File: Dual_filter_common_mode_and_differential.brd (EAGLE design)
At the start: 61 x 38.1 mm, 23 parts

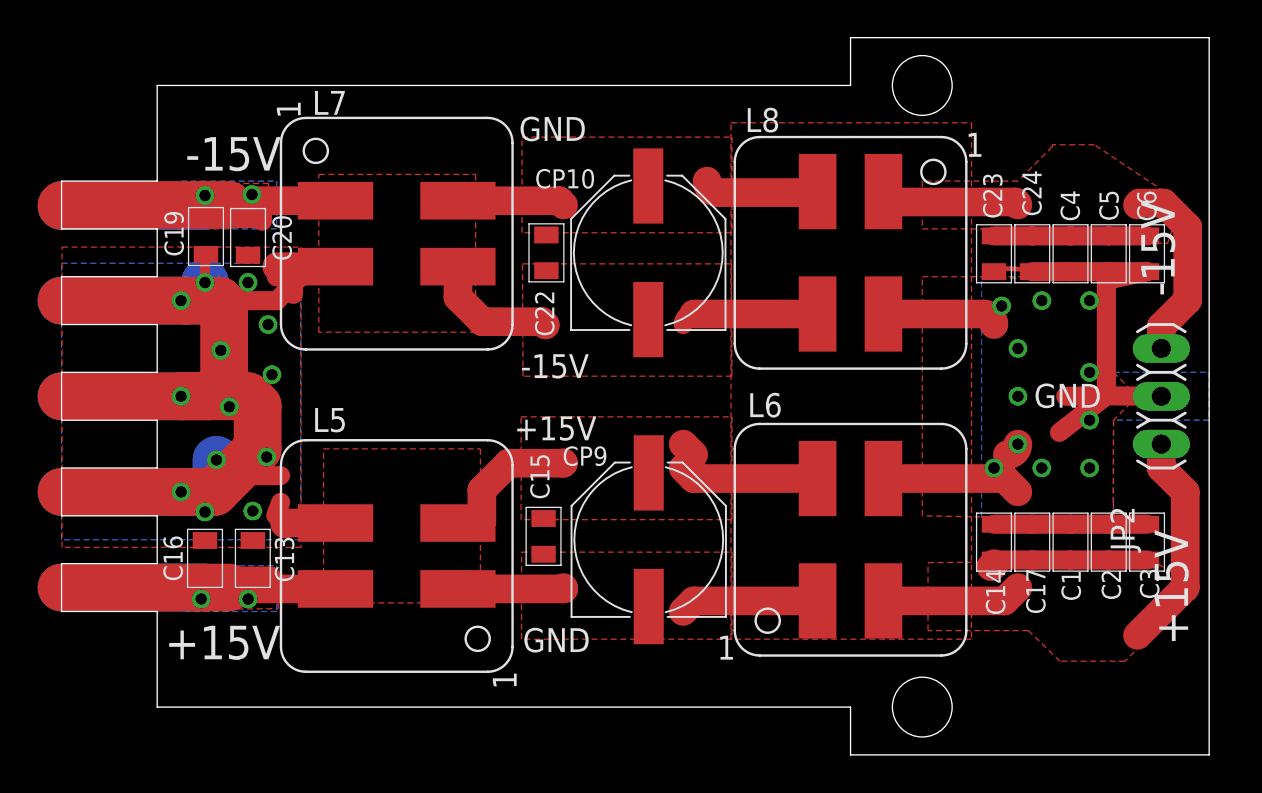
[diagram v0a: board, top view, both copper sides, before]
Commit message: Switched from CM-DIFF top CM-CM filtering
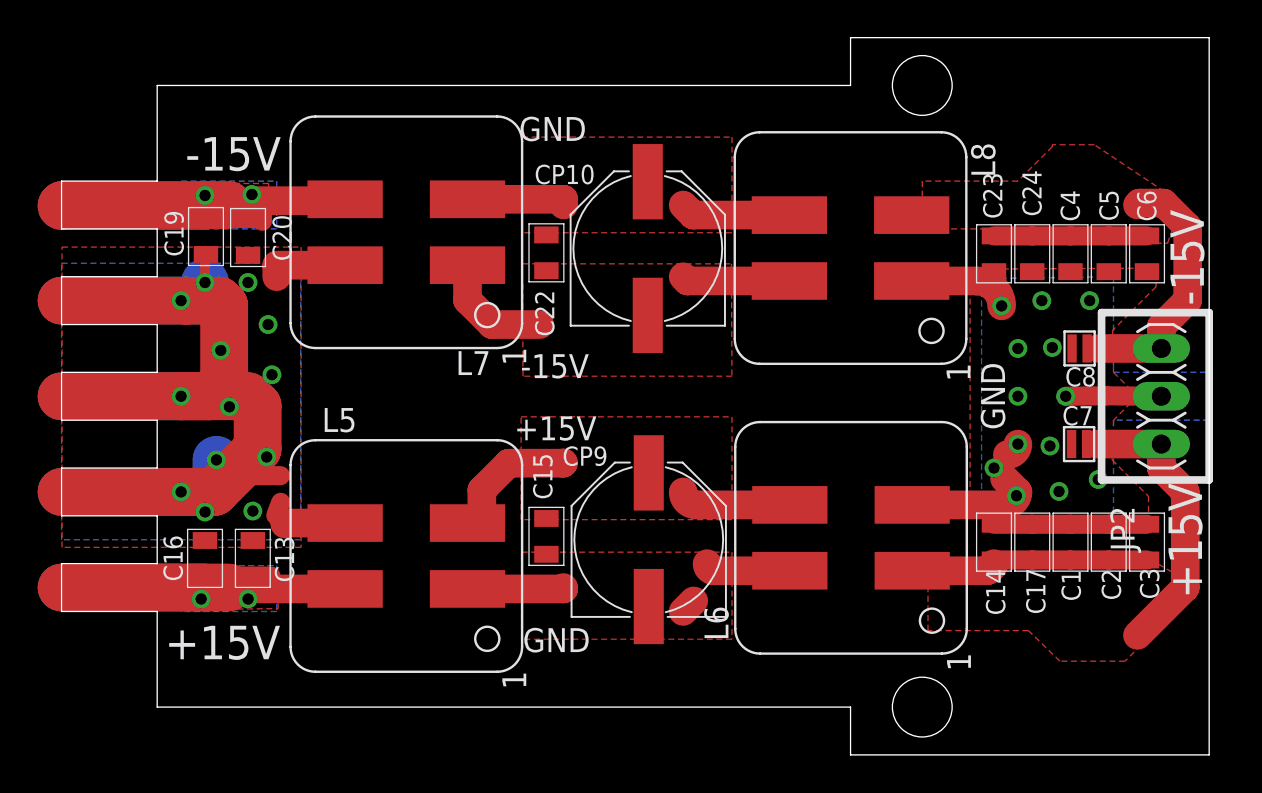
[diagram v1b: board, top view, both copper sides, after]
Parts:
- added C7, C8: 22nF, jqi_passives:C_MLCC_0306
- moved L7 0.51 mm to (19.6, 27.8), turned to 270 degrees
- moved L5 0.51 mm to (19.6, 10.6)
- moved L8 0.25 mm to (43.2, 26.9), turned to 270 degrees
- moved CP10 0.23 mm to (32.4, 26.9)
- moved C15 0.15 mm to (27.0, 11.6)
- moved L6 0.10 mm to (43.2, 11.5), turned to 270 degrees
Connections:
- net -15V2: now also L7.P$3; no longer L7.P$1
- net COM2: now also L7.P$4; no longer L7.P$2
- net GND2: now also C7.P$1, C8.P$2, L6.P$2, L8.P$1; no longer L6.P$3, L8.P$4
- net N$10: now also L7.P$1, L8.P$4; no longer L7.P$3, L8.P$3
- net N$13: now also C8.P$1, L8.P$2; no longer L8.P$1
- net N$6: now also L6.P$3; no longer L6.P$4
- net N$7: now also L6.P$4; no longer L6.P$1
- net N$9: now also L7.P$2, L8.P$3; no longer L7.P$4, L8.P$2
- net V+2: now also C7.P$2, L6.P$1; no longer L6.P$2
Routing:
- net GND2: track 49.4 -> 26.9 mm, vias 11 -> 13
- net COM2: track 84.3 -> 75.9 mm
- net N$6: track 17.0 -> 14.2 mm
- net N$7: track 14.0 -> 11.4 mm
- net N$13: track 26.3 -> 23.9 mm
- net N$10: track 14.3 -> 12.0 mm
- net V+2: track 27.5 -> 28.3 mm
- net N$9: track 11.9 -> 11.3 mm
- net +15V2: track 40.2 -> 40.8 mm
- removed copper zone on layer 1, net N$12
